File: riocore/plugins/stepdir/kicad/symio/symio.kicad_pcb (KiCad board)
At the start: 2 copper layers, 33.5 x 30.2 mm, 31 parts, among them J1 DE15_Pins_HighDensity, U1 MAX485E, U12 MAX485E, U17 ADuM1201BR, U2 MAX485E, U3 MAX485E, U4 MAX485E, U5 ADuM1201BR, U6 ADuM1201BR, U7 ADuM1201BR, U8 ADuM1201BR

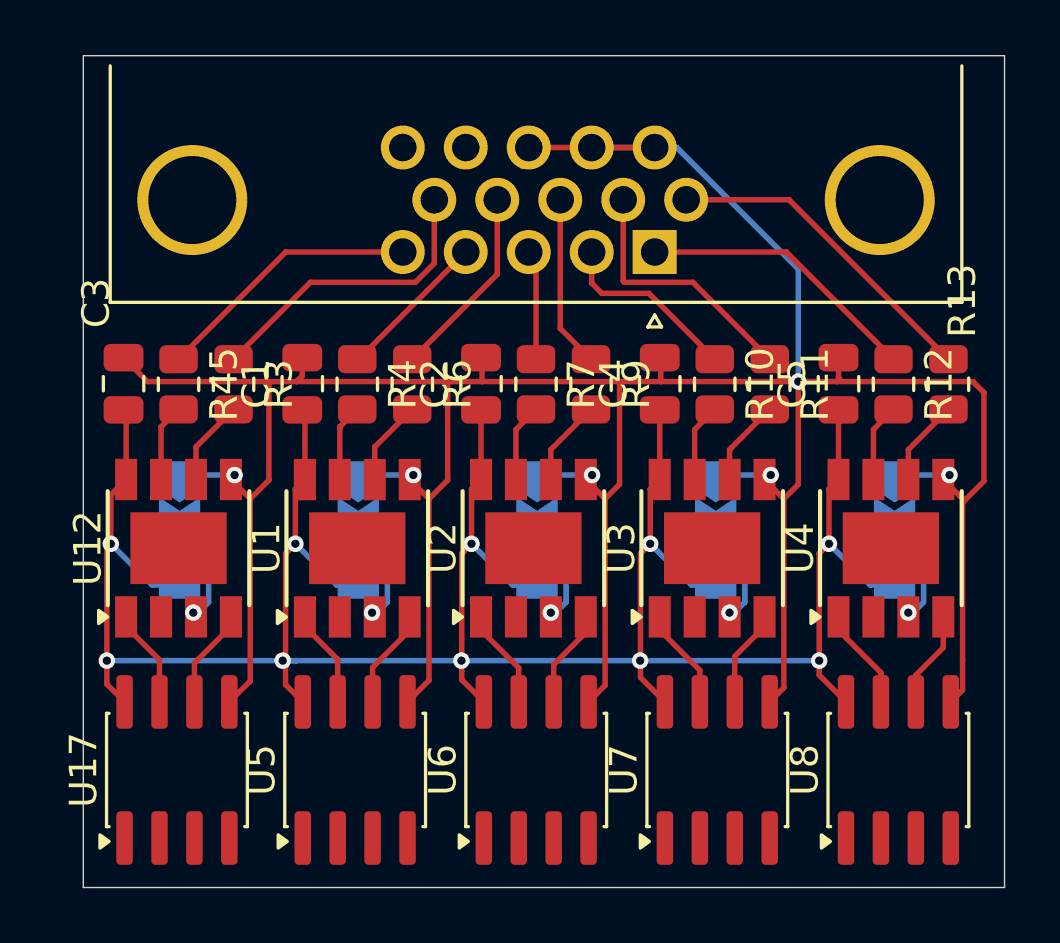
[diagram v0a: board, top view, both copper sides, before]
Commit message: kicad: pin positions
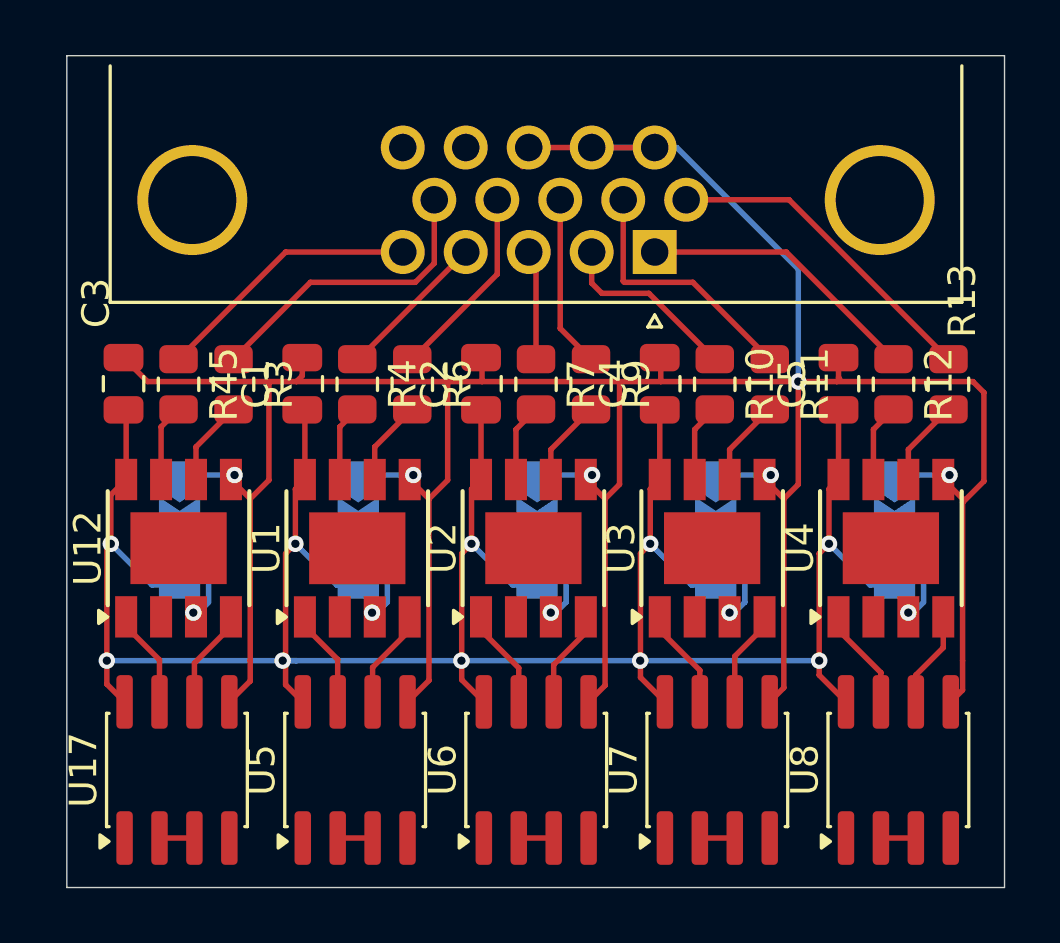
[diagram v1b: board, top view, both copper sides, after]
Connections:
- net /rxt1 renamed /step
- net /rxt2 renamed /dir
- net /rxt3 renamed /en
- net /rxt4 renamed /alarm
- net /rxt5 renamed /reset
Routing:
- net /reset: track 0.00 -> 1.27 mm
- net /dir: track 0.00 -> 1.27 mm
- net /alarm: track 0.00 -> 1.27 mm
- net /step: track 0.00 -> 1.27 mm
- net /en: track 0.00 -> 1.27 mm
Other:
- board size 33.5 x 30.2 mm -> 34.1 x 30.2 mm
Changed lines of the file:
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@@
 	(net 22 "Net-(J1-Pad10)")
 	(net 23 "Net-(J1-Pad6)")
-	(net 24 "/rxt1")
-	(net 25 "/rxt2")
-	(net 26 "/rxt3")
-	(net 27 "/rxt4")
-	(net 28 "/rxt5")
+	(net 24 "/dir")
+	(net 25 "/en")
+	(net 26 "/alarm")
+	(net 27 "/reset")
+	(net 28 "/step")
 	(net 29 "/rw2")
 	(net 30 "/rw3")
@@
 			(layers "F.Cu" "F.Mask" "F.Paste")
 			(roundrect_rratio 0.25)
-			(net 25 "/rxt2")
+			(net 24 "/dir")
 			(pinfunction "VOA")
 			(pintype "output")
@@
 			(layers "F.Cu" "F.Mask" "F.Paste")
 			(roundrect_rratio 0.25)
-			(net 25 "/rxt2")
+			(net 24 "/dir")
 			(pinfunction "VIB")
 			(pintype "input")
@@
 			(layers "F.Cu" "F.Mask" "F.Paste")
 			(roundrect_rratio 0.25)
-			(net 27 "/rxt4")
+			(net 26 "/alarm")
 			(pinfunction "VOA")
 			(pintype "output")
@@
 			(layers "F.Cu" "F.Mask" "F.Paste")
 			(roundrect_rratio 0.25)
-			(net 27 "/rxt4")
+			(net 26 "/alarm")
 			(pinfunction "VIB")
 			(pintype "input")
@@
 			(layers "F.Cu" "F.Mask" "F.Paste")
 			(roundrect_rratio 0.25)
-			(net 26 "/rxt3")
+			(net 25 "/en")
 			(pinfunction "VOA")
 			(pintype "output")
@@
 			(layers "F.Cu" "F.Mask" "F.Paste")
 			(roundrect_rratio 0.25)
-			(net 26 "/rxt3")
+			(net 25 "/en")
 			(pinfunction "VIB")
 			(pintype "input")
@@
 			(layers "F.Cu" "F.Mask" "F.Paste")
 			(roundrect_rratio 0.25)
-			(net 28 "/rxt5")
+			(net 27 "/reset")
 			(pinfunction "VOA")
 			(pintype "output")
@@
 			(layers "F.Cu" "F.Mask" "F.Paste")
 			(roundrect_rratio 0.25)
-			(net 28 "/rxt5")
+			(net 27 "/reset")
 			(pinfunction "VIB")
 			(pintype "input")
@@
 			(layers "F.Cu" "F.Mask" "F.Paste")
 			(roundrect_rratio 0.25)
-			(net 24 "/rxt1")
+			(net 28 "/step")
 			(pinfunction "VOA")
 			(pintype "output")
@@
 			(layers "F.Cu" "F.Mask" "F.Paste")
 			(roundrect_rratio 0.25)
-			(net 24 "/rxt1")
+			(net 28 "/step")
 			(pinfunction "VIB")
 			(pintype "input")
@@
 	)
 	(gr_rect
-		(start 142.5 87.25)
+		(start 141.9 87.25)
 		(end 176 117.5)
 		(stroke
@@
 	)
 	(segment
+		(start 151.75 115.7)
+		(end 153.02 115.7)
+		(width 0.2)
+		(layer "F.Cu")
+		(net 24)
+	)
+	(segment
+		(start 158.335 115.7)
+		(end 159.605 115.7)
+		(width 0.2)
+		(layer "F.Cu")
+		(net 25)
+	)
+	(segment
+		(start 164.92 115.7)
+		(end 166.19 115.7)
+		(width 0.2)
+		(layer "F.Cu")
+		(net 26)
+	)
+	(segment
+		(start 171.505 115.7)
+		(end 172.775 115.7)
+		(width 0.2)
+		(layer "F.Cu")
+		(net 27)
+	)
+	(segment
+		(start 145.27 115.7)
+		(end 146.54 115.7)
+		(width 0.2)
+		(layer "F.Cu")
+		(net 28)
+	)
+	(segment
